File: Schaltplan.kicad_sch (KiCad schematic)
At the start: 17 parts, among them K1 Relay, P1 USB Port vorheriger, P2 USB Port nächster, P4 USB Port Laden, U1 DC DC Wandler, U2 DC DC Wandler, U3 DS18B20, U4 Display, U5 DC DC Wandler, U6 Digitaler Poti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

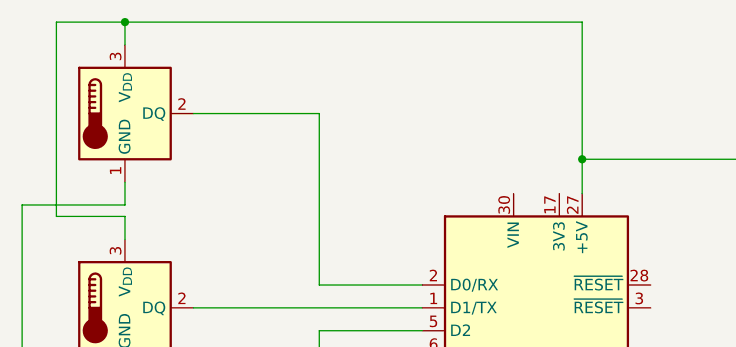
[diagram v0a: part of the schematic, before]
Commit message: Add Text Description Stuff
Co-authored-by: JumpStone <hi@jumpstone4477.de>
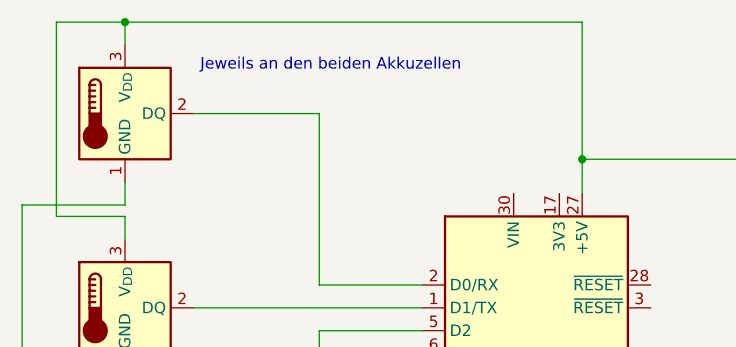
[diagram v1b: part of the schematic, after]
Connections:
- net at K1. (NC): now also A1.7 (D4)
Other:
- note added: "Jeweils an den beiden Akkuzellen"
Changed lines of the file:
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@@
 		(company "Akku-Craft")
+	)
+	(text "Jeweils an den beiden Akkuzellen"
+		(exclude_from_sim no)
+		(at 52.07 20.066 0)
+		(effects
+			(font
+				(size 1.27 1.27)
+			)
+		)
 	)
 	(junction
